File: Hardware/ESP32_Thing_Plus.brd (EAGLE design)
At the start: 66 x 31.8 mm, 46 parts, among them J1 455-1750-1-ND, J2 USB Female Type C Connector, J3 AUDIO_JACK_TRRSSMD_RA, Q2 MBT3904DW1T1, U2 ESP-WROOM-32NARROW, U3 AP2112K-3.3V, U4 CP2102N, U5 ADMP401

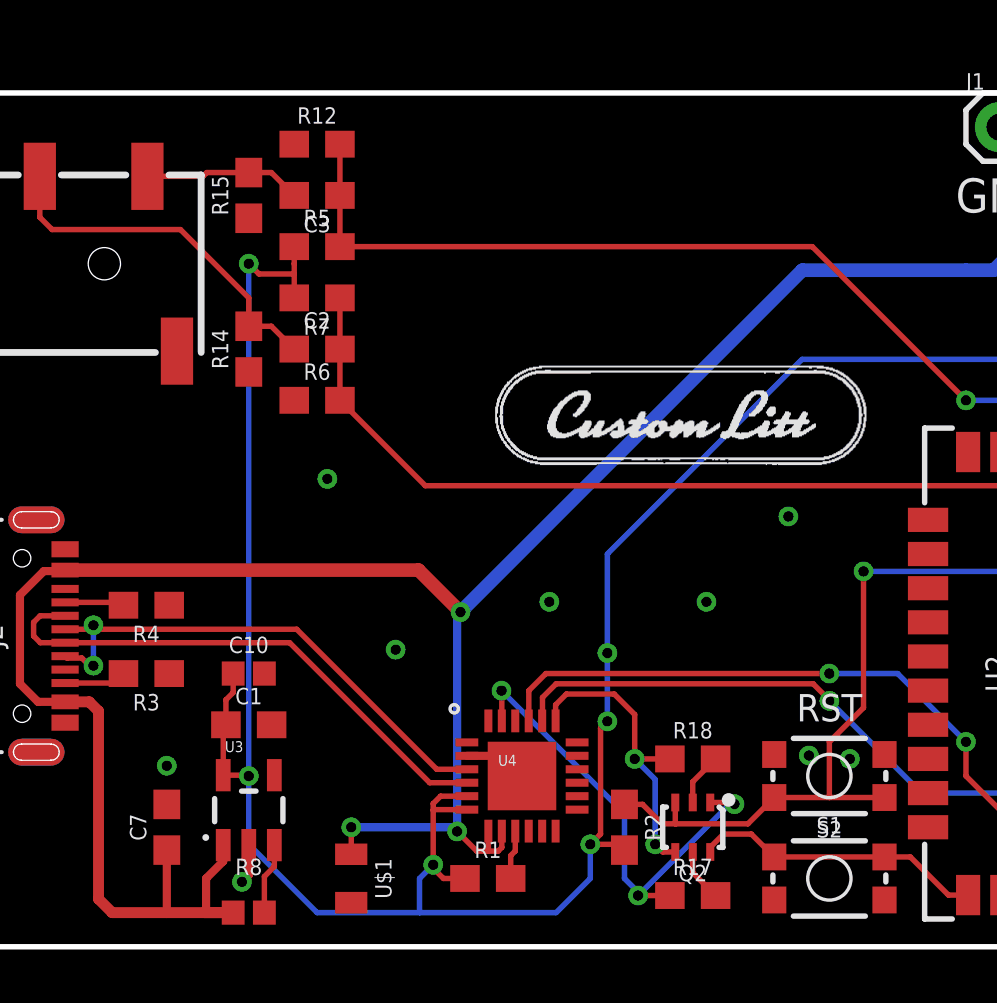
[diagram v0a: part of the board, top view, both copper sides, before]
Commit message: changing to 0603
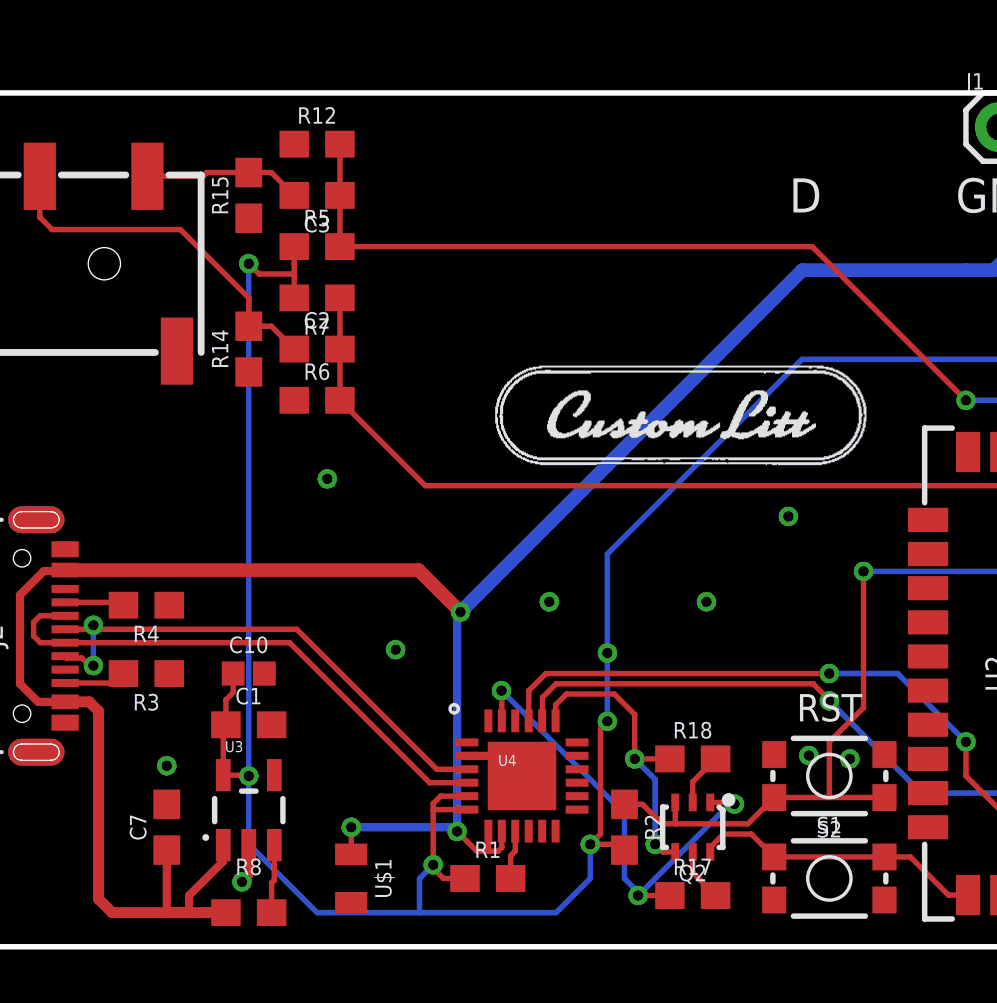
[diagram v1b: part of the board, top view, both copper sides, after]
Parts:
- R8: value 100K -> 100k; device SparkFun-Resistors:0402 -> SparkFun-Resistors:0603
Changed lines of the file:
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@@
 <setting verticaltext="up"/>
 </settings>
-<grid distance="10" unitdist="mm" unit="mm" style="lines" multiple="1" display="yes" altdistance="5" altunitdist="mil" altunit="inch"/>
+<grid distance="0.05" unitdist="inch" unit="inch" style="lines" multiple="1" display="yes" altdistance="5" altunitdist="mil" altunit="inch"/>
 <layers>
 <layer number="1" name="Top" color="4" fill="1" visible="yes" active="yes"/>
@@
 <layer number="25" name="tNames" color="7" fill="1" visible="yes" active="yes"/>
 <layer number="26" name="bNames" color="7" fill="1" visible="yes" active="yes"/>
-<layer number="27" name="tValues" color="7" fill="1" visible="yes" active="yes"/>
-<layer number="28" name="bValues" color="7" fill="1" visible="yes" active="yes"/>
+<layer number="27" name="tValues" color="7" fill="1" visible="no" active="yes"/>
+<layer number="28" name="bValues" color="7" fill="1" visible="no" active="yes"/>
 <layer number="29" name="tStop" color="7" fill="3" visible="no" active="yes"/>
 <layer number="30" name="bStop" color="7" fill="6" visible="no" active="yes"/>
@@
 <text x="40.259" y="27.305" size="1.27" layer="21" font="vector" ratio="15">GND</text>
 <text x="35.56" y="8.89" size="1.016" layer="21" font="vector" ratio="15" align="center">RST</text>
+<text x="34.069" y="27.305" size="1.27" layer="21" font="vector" ratio="15">D</text>
 </plain>
 <attributes>
@@
 <attribute name="VALUE" x="27.178" y="4.445" size="0.6096" layer="27" font="vector" ratio="20" rot="R270" align="top-center"/>
 </element>
-<element name="R8" library="SparkFun-Resistors" package="0402" value="100K" x="13.97" y="1.27" smashed="yes">
+<element name="R8" library="SparkFun-Resistors" package="0603" value="100k" x="13.97" y="1.27" smashed="yes">
 <attribute name="NAME" x="13.97" y="2.667" size="0.6096" layer="25" font="vector" ratio="20" align="bottom-center"/>
-<attribute name="PROD_ID" value="RES-13495" x="43.18" y="-43.18" size="1.778" layer="27" display="off"/>
-<attribute name="VALUE" x="13.97" y="0.508" size="0.6096" layer="27" font="vector" ratio="20" align="top-center"/>
+<attribute name="PROD_ID" value="RES-07828" x="43.18" y="-43.18" size="1.778" layer="27" display="off"/>
+<attribute name="VALUE" value="100k" x="13.97" y="0.508" size="0.6096" layer="27" font="vector" ratio="20" align="top-center"/>
 </element>
 <element name="S1" library="SparkFun-Switches" package="TACTILE_SWITCH_SMD_4.6X2.8MM" value="RESET" x="35.56" y="6.35" smashed="yes" rot="R180">
@@
 <wire x1="8.382" y1="1.778" x2="8.89" y2="1.27" width="0.4064" layer="1"/>
 <wire x1="8.89" y1="1.27" x2="10.922003125" y2="1.27" width="0.4064" layer="1"/>
-<wire x1="10.922003125" y1="1.27" x2="12.318996875" y2="1.27" width="0.4064" layer="1"/>
-<wire x1="12.318996875" y1="1.27" x2="13.39" y2="1.27" width="0.4064" layer="1"/>
+<wire x1="10.922003125" y1="1.27" x2="11.7475" y2="1.27" width="0.4064" layer="1"/>
+<wire x1="11.048996875" y1="1.27" x2="13.12" y2="1.27" width="0.4064" layer="1"/>
 <wire x1="21.717" y1="4.2898" x2="21.5618" y2="4.445" width="0.3048" layer="16"/>
 <wire x1="21.5618" y1="4.445" x2="17.78" y2="4.445" width="0.3048" layer="16"/>
@@
 <wire x1="20.283" y1="14.007" x2="21.844" y2="12.446" width="0.508" layer="1"/>
 <via x="21.844" y="12.446" extent="1-16" drill="0.381"/>
-<wire x1="12.319" y1="1.27" x2="13.39" y2="1.27" width="0.4064" layer="1"/>
+<wire x1="12.319" y1="1.27" x2="13.12" y2="1.27" width="0.4064" layer="1"/>
 <wire x1="46.99" y1="30.48" x2="41.6687" y2="25.1587" width="0.508" layer="16"/>
-<wire x1="12.3825" y1="2.54" x2="12.3825" y2="1.333503125" width="0.3048" layer="1"/>
-<wire x1="12.3825" y1="1.333503125" x2="12.318996875" y2="1.27" width="0.3048" layer="1"/>
-<wire x1="12.3825" y1="2.54" x2="13.02" y2="3.1775" width="0.3048" layer="1"/>
+<wire x1="11.7475" y1="1.905" x2="11.7475" y2="1.27" width="0.3048" layer="1"/>
+<wire x1="11.7475" y1="1.905" x2="13.02" y2="3.1775" width="0.3048" layer="1"/>
 <wire x1="13.02" y1="3.1775" x2="13.02" y2="3.81" width="0.3048" layer="1"/>
 <wire x1="10.922" y1="3.595" x2="10.922" y2="1.270003125" width="0.3048" layer="1"/>
 <wire x1="10.922" y1="1.270003125" x2="10.922003125" y2="1.27" width="0.3048" layer="1"/>
+<wire x1="10.922" y1="1.270003125" x2="11.048996875" y2="1.27" width="0" layer="19" extent="1-1"/>
 </signal>
 <signal name="D-">
@@
 <contactref element="U3" pad="3"/>
 <contactref element="R8" pad="2"/>
-<wire x1="14.92" y1="3.7799" x2="14.92" y2="2.982" width="0.2032" layer="1"/>
-<wire x1="14.55" y1="2.611996875" x2="14.92" y2="2.982" width="0.2032" layer="1"/>
-<wire x1="14.55" y1="1.27" x2="14.55" y2="2.611996875" width="0.2032" layer="1"/>
+<wire x1="14.82" y1="2.374" x2="14.82" y2="1.27" width="0.2032" layer="1"/>
+<wire x1="14.92" y1="3.7799" x2="14.92" y2="2.474" width="0.2032" layer="1"/>
+<wire x1="14.92" y1="2.474" x2="14.82" y2="2.374" width="0.2032" layer="1"/>
 </signal>
 <signal name="2">
